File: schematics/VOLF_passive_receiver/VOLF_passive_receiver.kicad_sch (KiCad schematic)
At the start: 4 parts, among them J1 AudioJack3

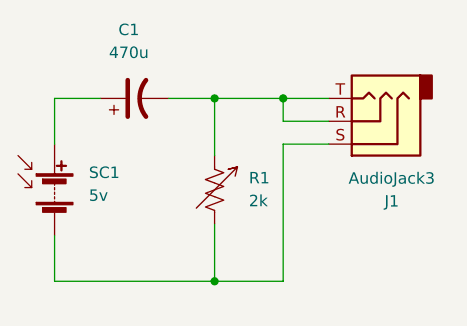
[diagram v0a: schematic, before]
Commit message: changed MCU pin assignments and added schematics for MCU enhanced circuits
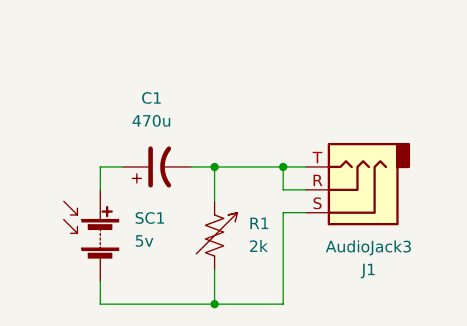
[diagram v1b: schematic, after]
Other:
- moved on the sheet: C1, J1, R1, SC1
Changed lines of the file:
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@@
 	)
 	(junction
-		(at 109.22 53.34)
+		(at 109.22 60.96)
 		(diameter 0)
 		(color 0 0 0 0)
 	)
 	(junction
-		(at 101.6 73.66)
+		(at 101.6 76.2)
 		(diameter 0)
 		(color 0 0 0 0)
 	)
 	(junction
-		(at 101.6 53.34)
+		(at 101.6 60.96)
 		(diameter 0)
 		(color 0 0 0 0)
@@
 	(wire
 		(pts
-			(xy 88.9 53.34) (xy 83.82 53.34)
-		)
-		(stroke
-			(width 0)
-			(type default)
-		)
-	)
-	(wire
-		(pts
-			(xy 101.6 53.34) (xy 101.6 59.69)
-		)
-		(stroke
-			(width 0)
-			(type default)
-		)
-	)
-	(wire
-		(pts
-			(xy 109.22 53.34) (xy 109.22 55.88)
-		)
-		(stroke
-			(width 0)
-			(type default)
-		)
-	)
-	(wire
-		(pts
-			(xy 114.3 55.88) (xy 109.22 55.88)
-		)
-		(stroke
-			(width 0)
-			(type default)
-		)
-	)
-	(wire
-		(pts
-			(xy 101.6 73.66) (xy 109.22 73.66)
-		)
-		(stroke
-			(width 0)
-			(type default)
-		)
-	)
-	(wire
-		(pts
-			(xy 101.6 53.34) (xy 109.22 53.34)
-		)
-		(stroke
-			(width 0)
-			(type default)
-		)
-	)
-	(wire
-		(pts
-			(xy 109.22 58.42) (xy 109.22 73.66)
-		)
-		(stroke
-			(width 0)
-			(type default)
-		)
-	)
-	(wire
-		(pts
-			(xy 83.82 73.66) (xy 101.6 73.66)
-		)
-		(stroke
-			(width 0)
-			(type default)
-		)
-	)
-	(wire
-		(pts
-			(xy 83.82 68.58) (xy 83.82 73.66)
-		)
-		(stroke
-			(width 0)
-			(type default)
-		)
-	)
-	(wire
-		(pts
-			(xy 96.52 53.34) (xy 101.6 53.34)
-		)
-		(stroke
-			(width 0)
-			(type default)
-		)
-	)
-	(wire
-		(pts
-			(xy 101.6 73.66) (xy 101.6 67.31)
-		)
-		(stroke
-			(width 0)
-			(type default)
-		)
-	)
-	(wire
-		(pts
-			(xy 114.3 58.42) (xy 109.22 58.42)
-		)
-		(stroke
-			(width 0)
-			(type default)
-		)
-	)
-	(wire
-		(pts
-			(xy 83.82 53.34) (xy 83.82 58.42)
-		)
-		(stroke
-			(width 0)
-			(type default)
-		)
-	)
-	(wire
-		(pts
-			(xy 109.22 53.34) (xy 114.3 53.34)
+			(xy 101.6 60.96) (xy 109.22 60.96)
+		)
+		(stroke
+			(width 0)
+			(type default)
+		)
+	)
+	(wire
+		(pts
+			(xy 91.44 60.96) (xy 88.9 60.96)
+		)
+		(stroke
+			(width 0)
+			(type default)
+		)
+	)
+	(wire
+		(pts
+			(xy 109.22 60.96) (xy 109.22 63.5)
+		)
+		(stroke
+			(width 0)
+			(type default)
+		)
+	)
+	(wire
+		(pts
+			(xy 101.6 60.96) (xy 101.6 64.77)
+		)
+		(stroke
+			(width 0)
+			(type default)
+		)
+	)
+	(wire
+		(pts
+			(xy 109.22 60.96) (xy 111.76 60.96)
+		)
+		(stroke
+			(width 0)
+			(type default)
+		)
+	)
+	(wire
+		(pts
+			(xy 111.76 63.5) (xy 109.22 63.5)
+		)
+		(stroke
+			(width 0)
+			(type default)
+		)
+	)
+	(wire
+		(pts
+			(xy 109.22 66.04) (xy 109.22 76.2)
+		)
+		(stroke
+			(width 0)
+			(type default)
+		)
+	)
+	(wire
+		(pts
+			(xy 88.9 76.2) (xy 101.6 76.2)
+		)
+		(stroke
+			(width 0)
+			(type default)
+		)
+	)
+	(wire
+		(pts
+			(xy 88.9 73.66) (xy 88.9 76.2)
+		)
+		(stroke
+			(width 0)
+			(type default)
+		)
+	)
+	(wire
+		(pts
+			(xy 99.06 60.96) (xy 101.6 60.96)
+		)
+		(stroke
+			(width 0)
+			(type default)
+		)
+	)
+	(wire
+		(pts
+			(xy 101.6 76.2) (xy 109.22 76.2)
+		)
+		(stroke
+			(width 0)
+			(type default)
+		)
+	)
+	(wire
+		(pts
+			(xy 101.6 76.2) (xy 101.6 72.39)
+		)
+		(stroke
+			(width 0)
+			(type default)
+		)
+	)
+	(wire
+		(pts
+			(xy 111.76 66.04) (xy 109.22 66.04)
+		)
+		(stroke
+			(width 0)
+			(type default)
+		)
+	)
+	(wire
+		(pts
+			(xy 88.9 60.96) (xy 88.9 63.5)
 		)
 		(stroke
@@
 	(symbol
 		(lib_id "Connector_Audio:AudioJack3")
-		(at 119.38 55.88 180)
+		(at 116.84 63.5 180)
 		(unit 1)
 		(exclude_from_sim no)
@@
 		(fields_autoplaced yes)
 		(property "Reference" "J1"
-			(at 121.285 64.77 0)
+			(at 118.745 72.39 0)
 			(effects
 				(font
@@
 		)
 		(property "Value" "AudioJack3"
-			(at 121.285 62.23 0)
+			(at 118.745 69.85 0)
 			(effects
 				(font
@@
 		)
 		(property "Footprint" ""
-			(at 119.38 55.88 0)
+			(at 116.84 63.5 0)
 			(effects
 				(font
@@
 		)
 		(property "Datasheet" "~"
-			(at 119.38 55.88 0)
+			(at 116.84 63.5 0)
 			(effects
 				(font
@@
 		)
 		(property "Description" "Audio Jack, 3 Poles (Stereo / TRS)"
-			(at 119.38 55.88 0)
+			(at 116.84 63.5 0)
 			(effects
 				(font
@@
 	(symbol
 		(lib_id "Device:Solar_Cells")
-		(at 83.82 63.5 0)
+		(at 88.9 68.58 0)
 		(unit 1)
 		(exclude_from_sim no)
@@
 		(fields_autoplaced yes)
 		(property "Reference" "SC1"
-			(at 87.63 61.5949 0)
+			(at 92.71 66.6749 0)
 			(effects
 				(font
@@
 		)
 		(property "Value" "5v"
-			(at 87.63 64.1349 0)
+			(at 92.71 69.2149 0)
 			(effects
 				(font
@@
 		)
 		(property "Footprint" ""
-			(at 83.82 61.976 90)
+			(at 88.9 67.056 90)
 			(effects
 				(font
@@
 		)
 		(property "Datasheet" "~"
-			(at 83.82 61.976 90)
+			(at 88.9 67.056 90)
 			(effects
 				(font
@@
 		)
 		(property "Description" "Multiple solar cells"
-			(at 83.82 63.5 0)
+			(at 88.9 68.58 0)
 			(effects
 				(font
@@
 	(symbol
 		(lib_id "Device:R_Variable_US")
-		(at 101.6 63.5 0)
+		(at 101.6 68.58 0)
 		(unit 1)
 		(exclude_from_sim no)
@@
 		(fields_autoplaced yes)
 		(property "Reference" "R1"
-			(at 105.41 62.1918 0)
+			(at 105.41 67.2718 0)
 			(effects
 				(font
@@
 		)
 		(property "Value" "2k"
-			(at 105.41 64.7318 0)
+			(at 105.41 69.8118 0)
 			(effects
 				(font
@@
 		)
 		(property "Footprint" ""
-			(at 99.822 63.5 90)
+			(at 99.822 68.58 90)
 			(effects
 				(font
@@
 		)
 		(property "Datasheet" "~"
-			(at 101.6 63.5 0)
+			(at 101.6 68.58 0)
 			(effects
 				(font
@@
 		)
 		(property "Description" "Variable resistor, US symbol"
-			(at 101.6 63.5 0)
+			(at 101.6 68.58 0)
 			(effects
 				(font
@@
 	(symbol
 		(lib_id "Device:C_Polarized_US")
-		(at 92.71 53.34 90)
+		(at 95.25 60.96 90)
 		(unit 1)
 		(exclude_from_sim no)
@@
 		(fields_autoplaced yes)
 		(property "Reference" "C1"
-			(at 92.075 45.72 90)
+			(at 94.615 53.34 90)
 			(effects
 				(font
@@
 		)
 		(property "Value" "470u"
-			(at 92.075 48.26 90)
+			(at 94.615 55.88 90)
 			(effects
 				(font
@@
 		)
 		(property "Footprint" ""
-			(at 92.71 53.34 0)
+			(at 95.25 60.96 0)
 			(effects
 				(font
@@
 		)
 		(property "Datasheet" "~"
-			(at 92.71 53.34 0)
+			(at 95.25 60.96 0)
 			(effects
 				(font
@@
 		)
 		(property "Description" "Polarized capacitor, US symbol"
-			(at 92.71 53.34 0)
-			(effects
-				(font
+			(at 95.25 60.96 0)
+			(effects
+				(font
